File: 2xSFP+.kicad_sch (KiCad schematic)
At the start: 31 parts, among them J4 SFP+_Bel_SS-79100-010

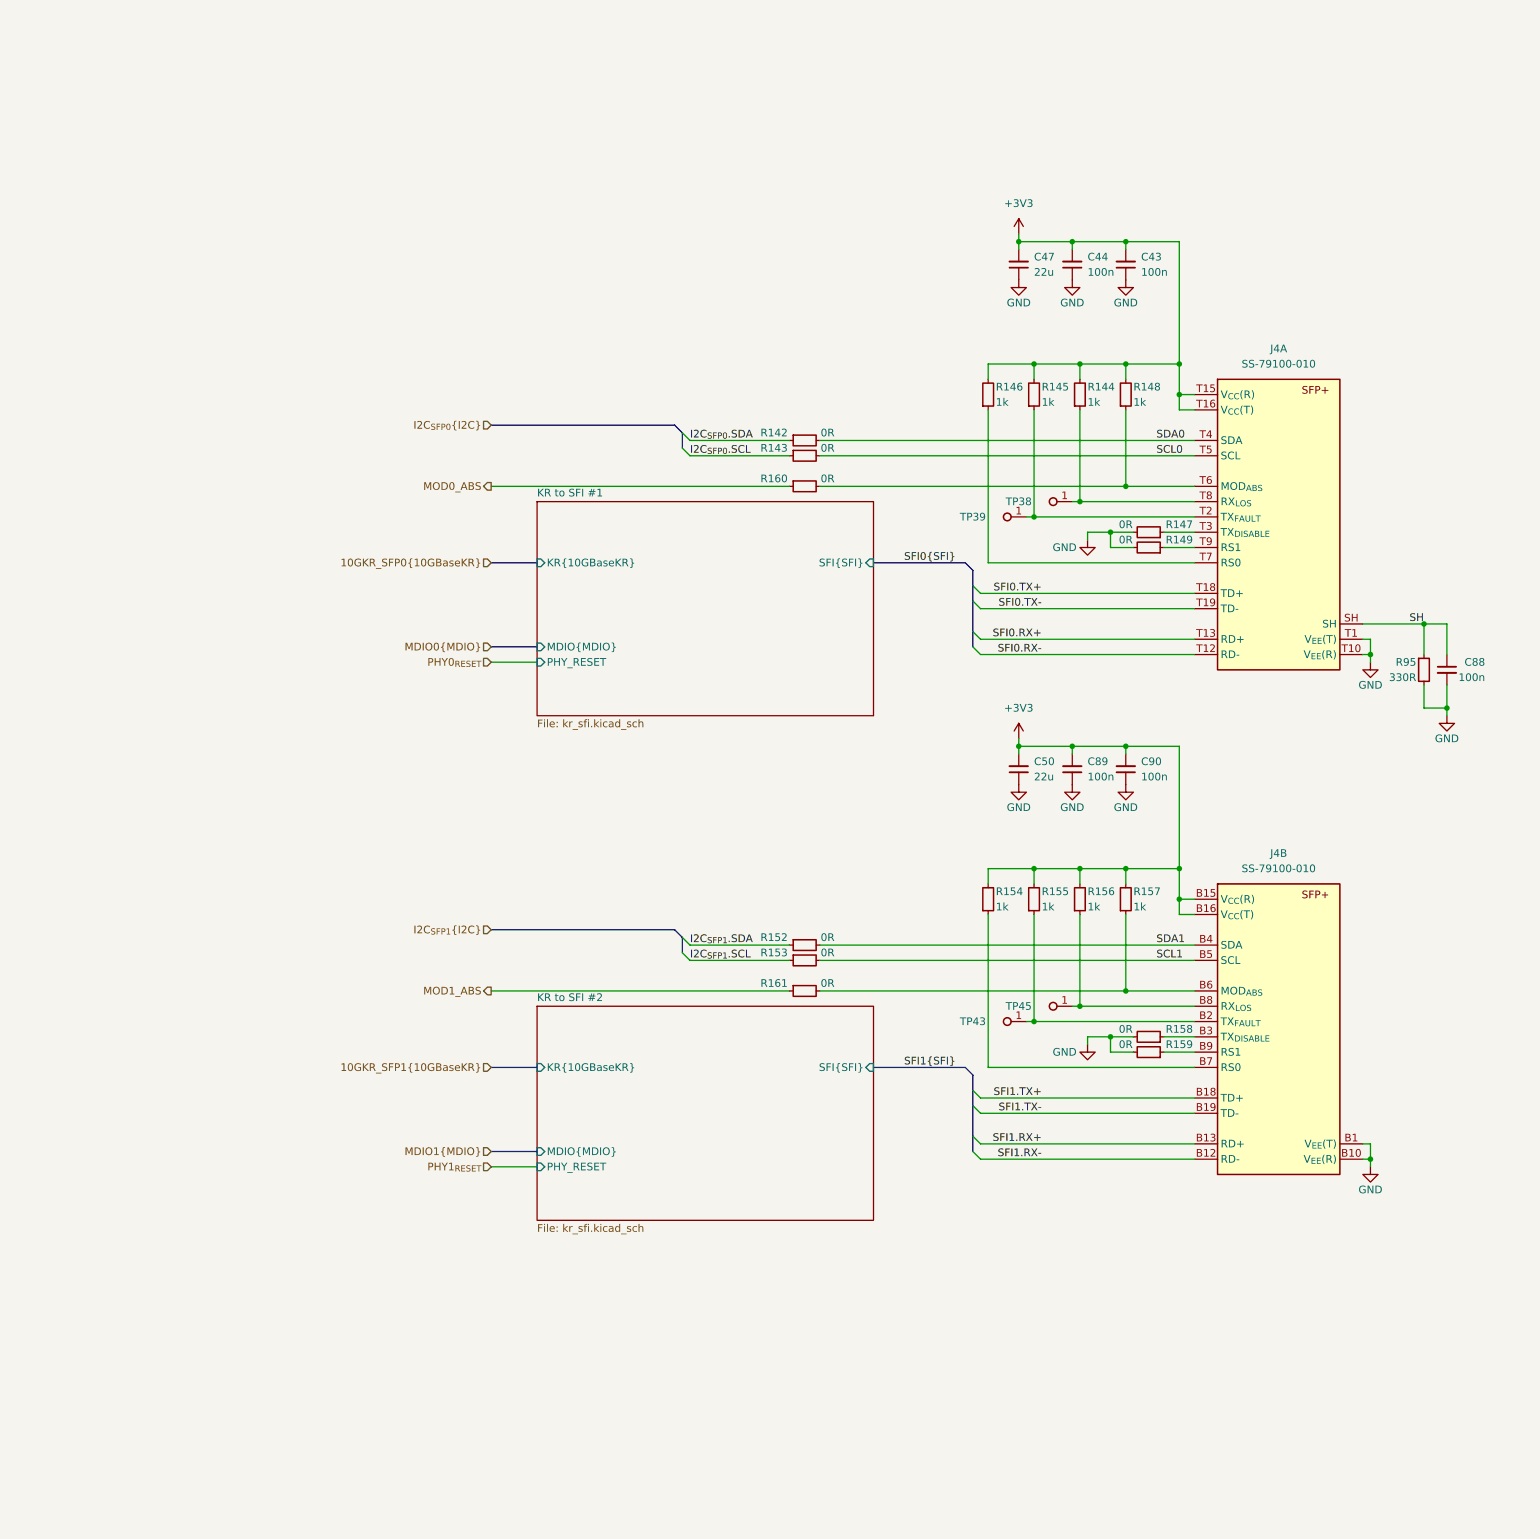
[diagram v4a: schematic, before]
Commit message: [#57498] Add SFP+ indicator LEDs
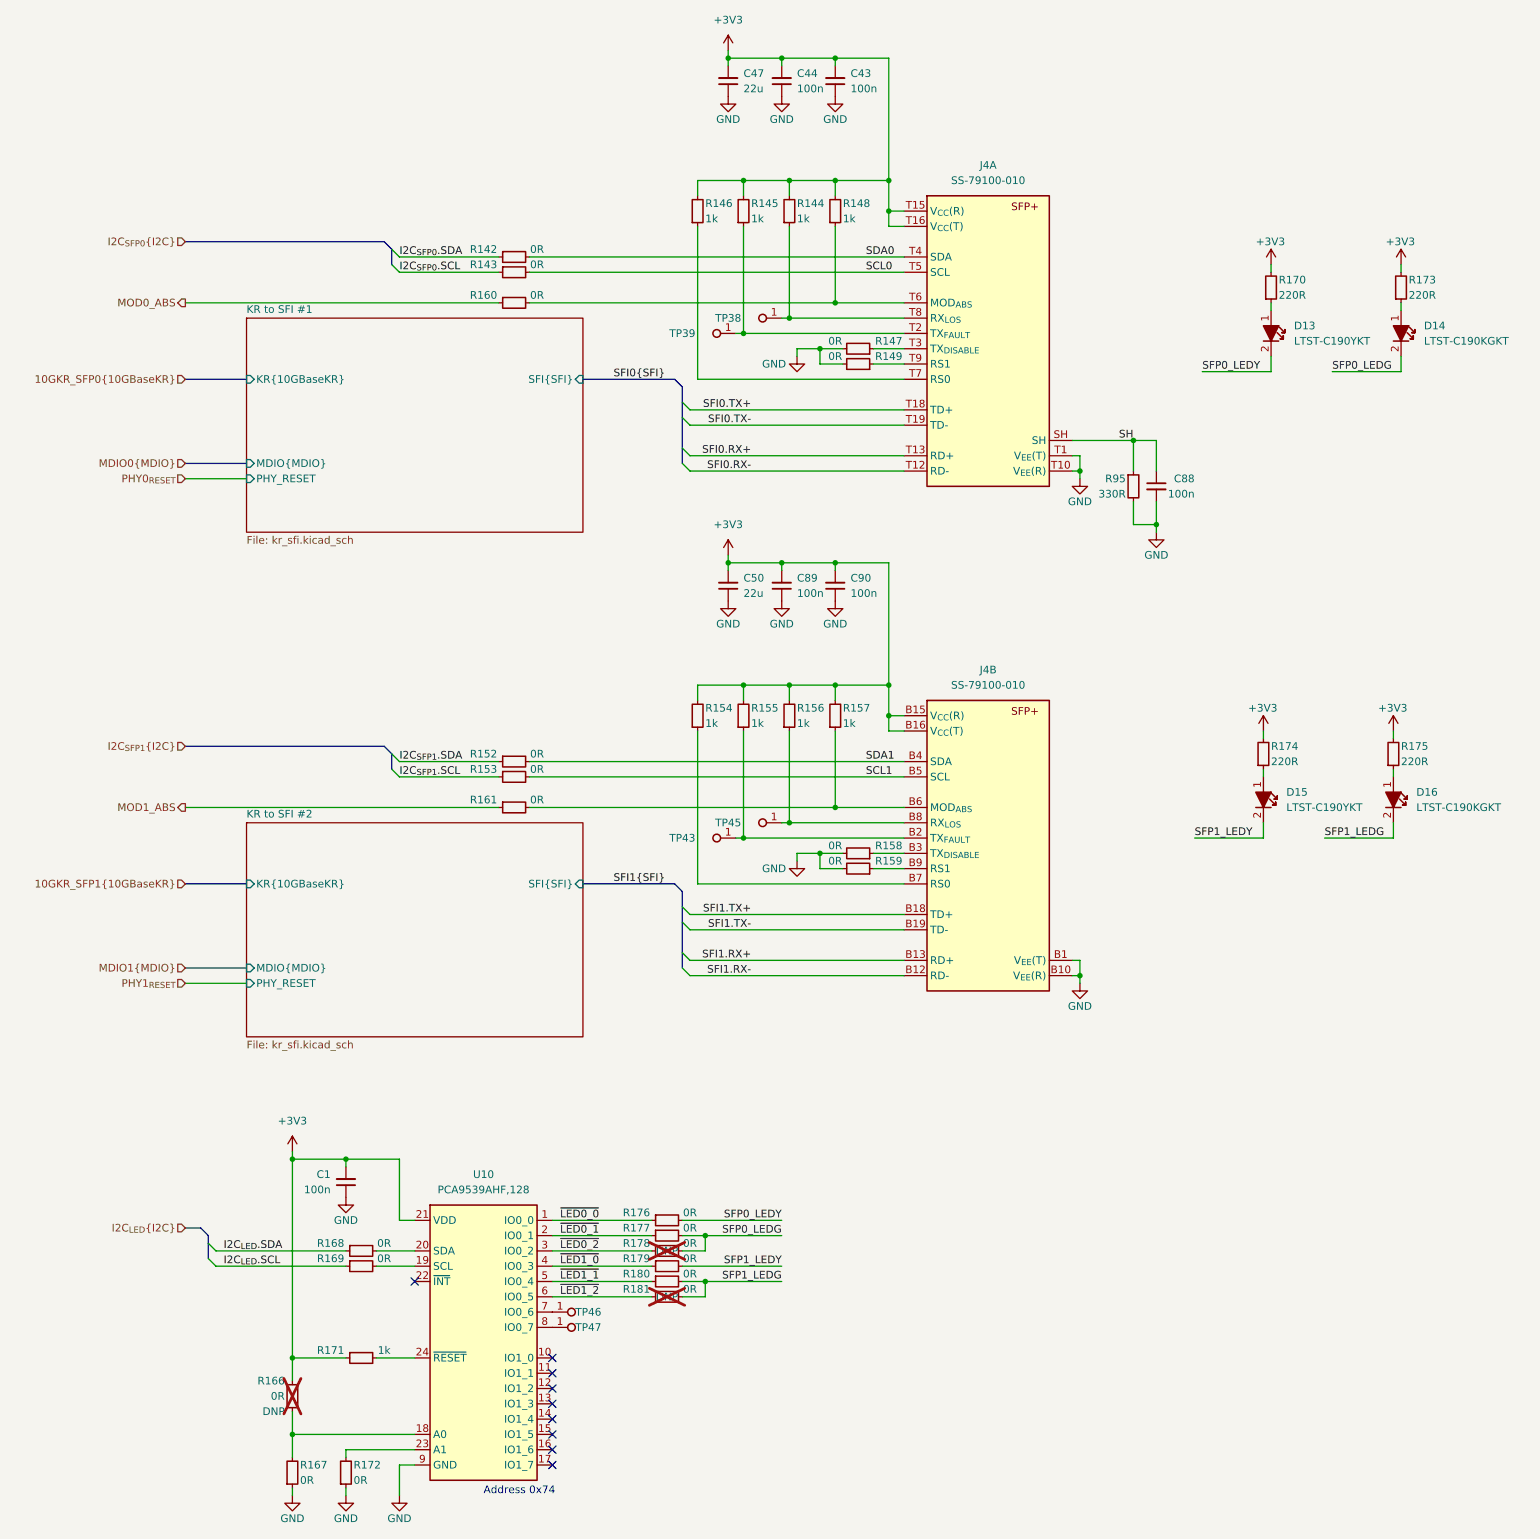
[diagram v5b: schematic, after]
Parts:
- added C1: C_100n_0402, antmicro-footprints:C_0402_1005Metric, symbol antmicroCapacitors0402:C_100n_0402
- added D13, D15: LED_Y_0603_LTST-C190YKT, antmicro-footprints:LED_0603_1608Metric_G, symbol antmicroLEDIndicationDiscrete:LED_Y_0603_LTST-C190YKT
- added D14, D16: LED_G_0603_LTST-C190KGKT, antmicro-footprints:LED_0603_1608Metric_G, symbol antmicroLEDIndicationDiscrete:LED_G_0603_LTST-C190KGKT
- added R166, R167, R168, R169, R172, R176, R177, R178, R179, R180, R181: R_0R_0402, antmicro-footprints:R_0402_1005Metric, symbol antmicroResistors0402:R_0R_0402
- added R170, R173, R174, R175: R_220R_0402, antmicro-footprints:R_0402_1005Metric, symbol antmicroResistors0402:R_220R_0402
- added R171: R_1k_0402, antmicro-footprints:R_0402_1005Metric, symbol antmicroResistors0402:R_1k_0402
- added TP46, TP47: TP_0.75mm_SMD, antmicro-footprints:TP_SMD_0.75mm, symbol antmicroTestPoints:TP_0.75mm_SMD
- added U10: PCA9539AHF, antmicro-footprints:QFN-24-1EP_4x4mm_P0.5_EP2.1x2.1mm, symbol antmicroInterfaceIOExpanders:PCA9539AHF
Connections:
- net +3V3: now also C1.2, R166.2, R170.2, R171.1, R173.2, R174.2, R175.2, U10.21 (VDD)
- net GND: now also C1.1, R167.1, R172.1, U10.25 (GND), U10.9 (GND)
- new net: R166.1, R167.2, U10.18 (A0)
- new net: R169.2, U10.19 (SCL)
- new net: R168.2, U10.20 (SDA)
- new net: R172.2, U10.23 (A1)
- new net: R171.2, U10.24 (~{RESET})
- new net: TP46.1, U10.7 (IO0_6)
- new net: TP47.1, U10.8 (IO0_7)
- new net: D13.1, R170.1
- new net: D14.1, R173.1
- new net: D15.1, R174.1
- new net: D16.1, R175.1
- new net I2C_{LED}.SCL: R169.1
- new net I2C_{LED}.SDA: R168.1
- new net SFP0_LEDG: D14.2, R177.2, R178.2
- new net SFP0_LEDY: D13.2, R176.2
- new net SFP1_LEDG: D16.2, R180.2, R181.2
- new net SFP1_LEDY: D15.2, R179.2
- new net ~{LED0_0}: R176.1, U10.1 (IO0_0)
- new net ~{LED0_1}: R177.1, U10.2 (IO0_1)
- new net ~{LED0_2}: R178.1, U10.3 (IO0_2)
- new net ~{LED1_0}: R179.1, U10.4 (IO0_3)
- new net ~{LED1_1}: R180.1, U10.5 (IO0_4)
- new net ~{LED1_2}: R181.1, U10.6 (IO0_5)
- no-connect marks 0 -> 9
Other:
- note added: "Address 0x74"
- moved on the sheet: C43, C44, C47, C50, C88, C89, C90, J4A, J4B, R142, R143, R144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

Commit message: [#58137] Update backplane connector pinout
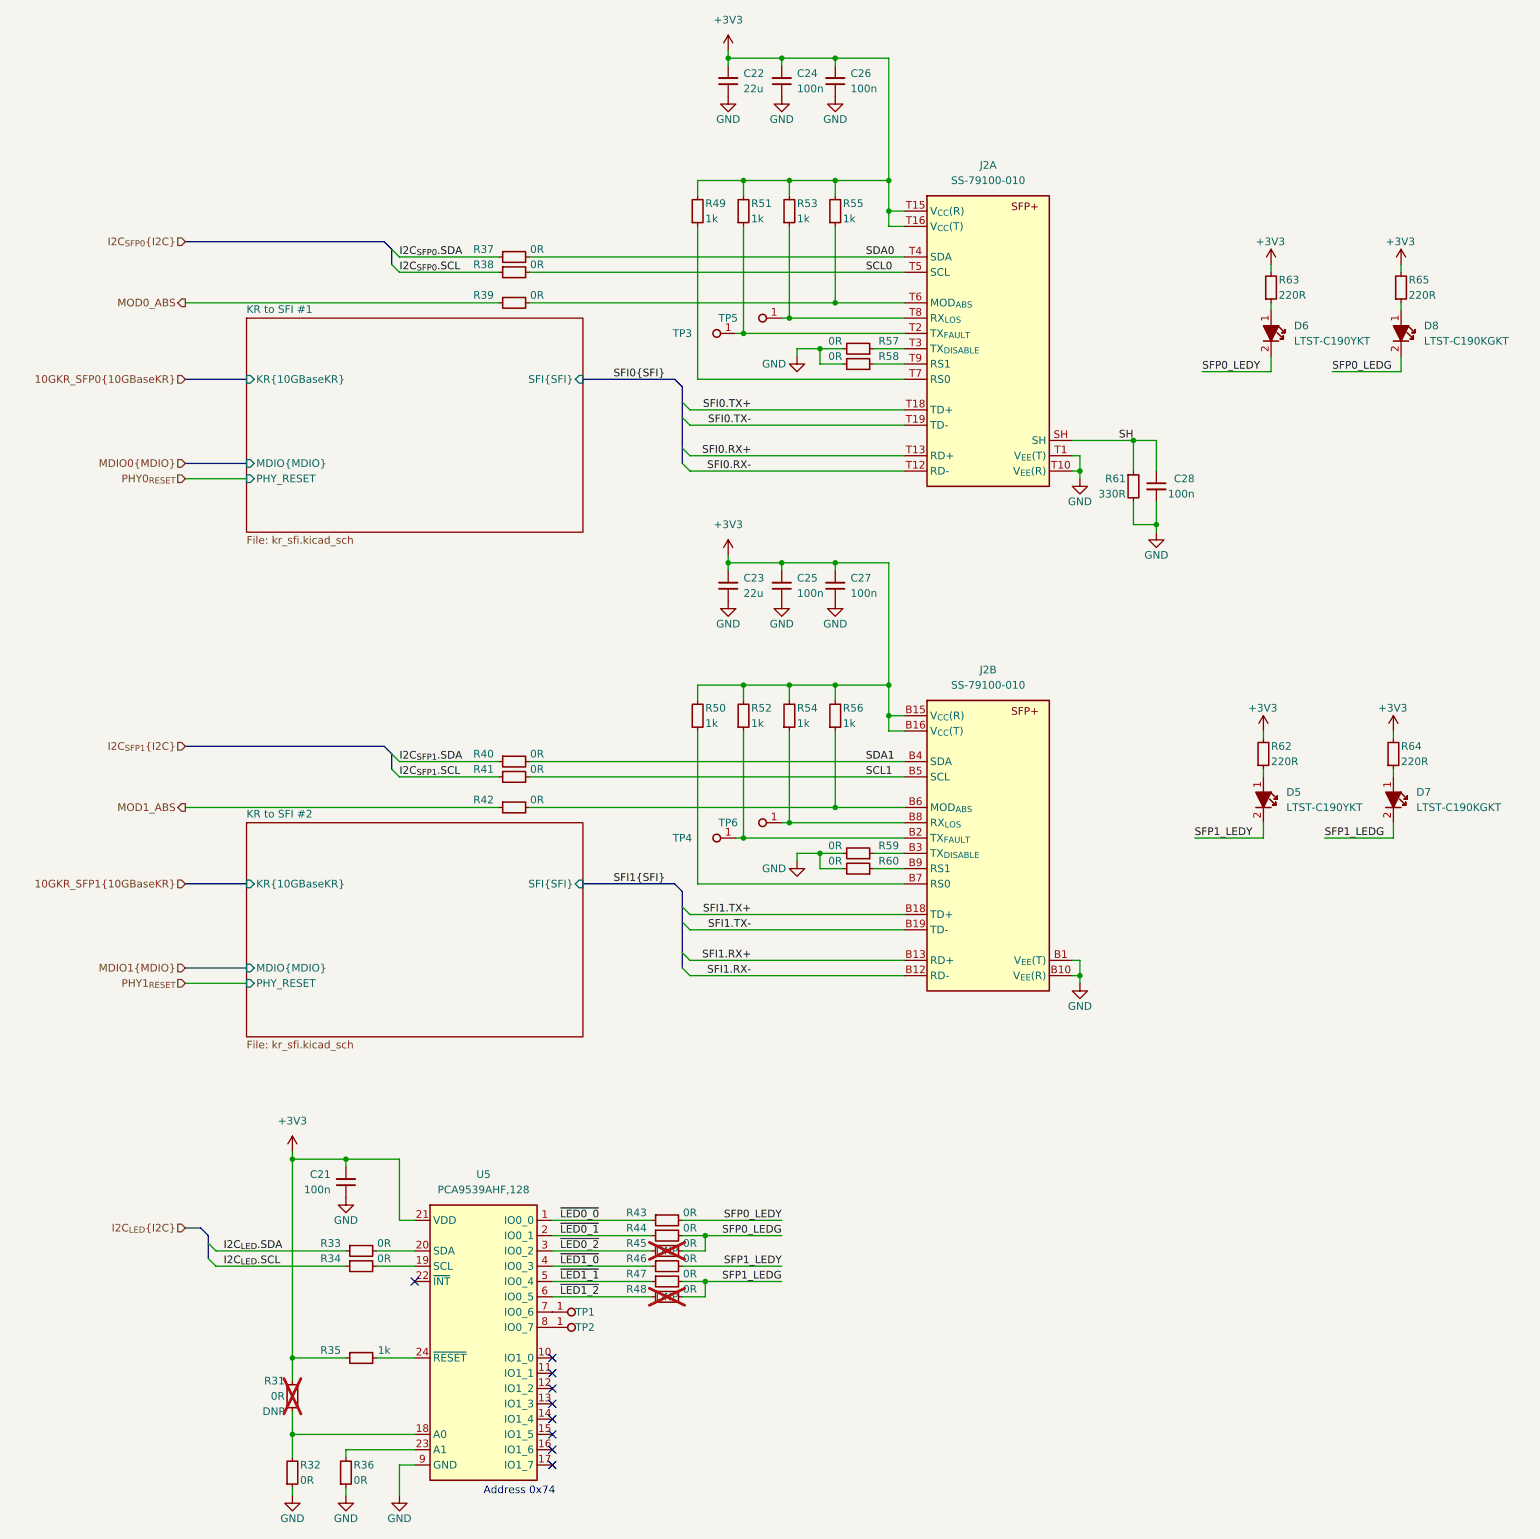
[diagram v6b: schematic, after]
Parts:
- renumbered C1 to C21, C47 to C22, C50 to C23, C44 to C24, C89 to C25, C43 to C26, C90 to C27, C88 to C28, D15 to D5, D13 to D6, D16 to D7, D14 to D8, J4 to J2, R166 to R31, R167 to R32, R168 to R33, R169 to R34, R171 to R35, R172 to R36, R142 to R37, R143 to R38, R160 to R39, R152 to R40, R153 to R41, R161 to R42, R176 to R43, R177 to R44, R178 to R45, R179 to R46, R180 to R47, R181 to R48, R146 to R49, R154 to R50, R145 to R51, R155 to R52, R144 to R53, R156 to R54, R148 to R55, R157 to R56, R147 to R57, R149 to R58, R158 to R59, R159 to R60, R95 to R61, R174 to R62, R170 to R63, R175 to R64, R173 to R65, TP46 to TP1, TP47 to TP2, TP39 to TP3, TP43 to TP4, TP38 to TP5, TP45 to TP6, U10 to U5
